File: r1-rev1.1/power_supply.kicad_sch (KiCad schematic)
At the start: 26 parts, among them J1 GT-BTP30003-xxxA-16A, Q2 AO3401A, U1 LM66100DCK, U2 TPS62A01DRLR, U3 TPS62A01DRLR, U4 XC6206P33xMR, U5 TP4057

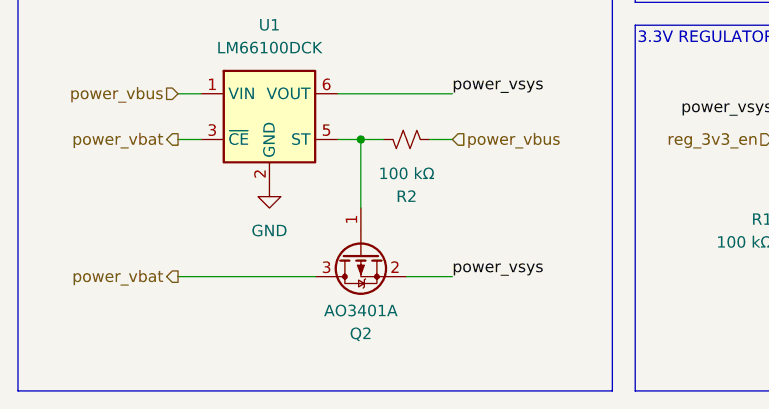
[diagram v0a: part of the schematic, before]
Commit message: Fix symbol library links & resync footprints from KiCAD libraries
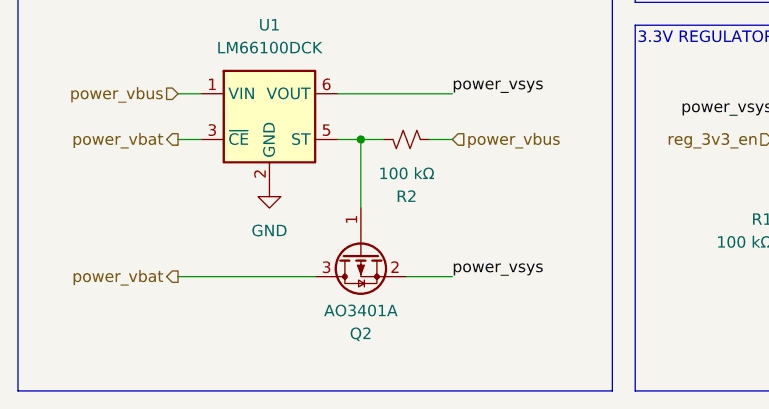
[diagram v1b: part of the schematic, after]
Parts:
- Q2: symbol Device:Q_PMOS_GSD -> Transistor_FET:Q_PMOS_GSD
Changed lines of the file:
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@@
 	)
 	(symbol
-		(lib_id "Device:Q_PMOS_GSD")
+		(lib_id "Transistor_FET:Q_PMOS_GSD")
 		(at 66.04 109.22 90)
 		(mirror x)
